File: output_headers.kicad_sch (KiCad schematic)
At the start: 1 part, among them J3 171857-0003

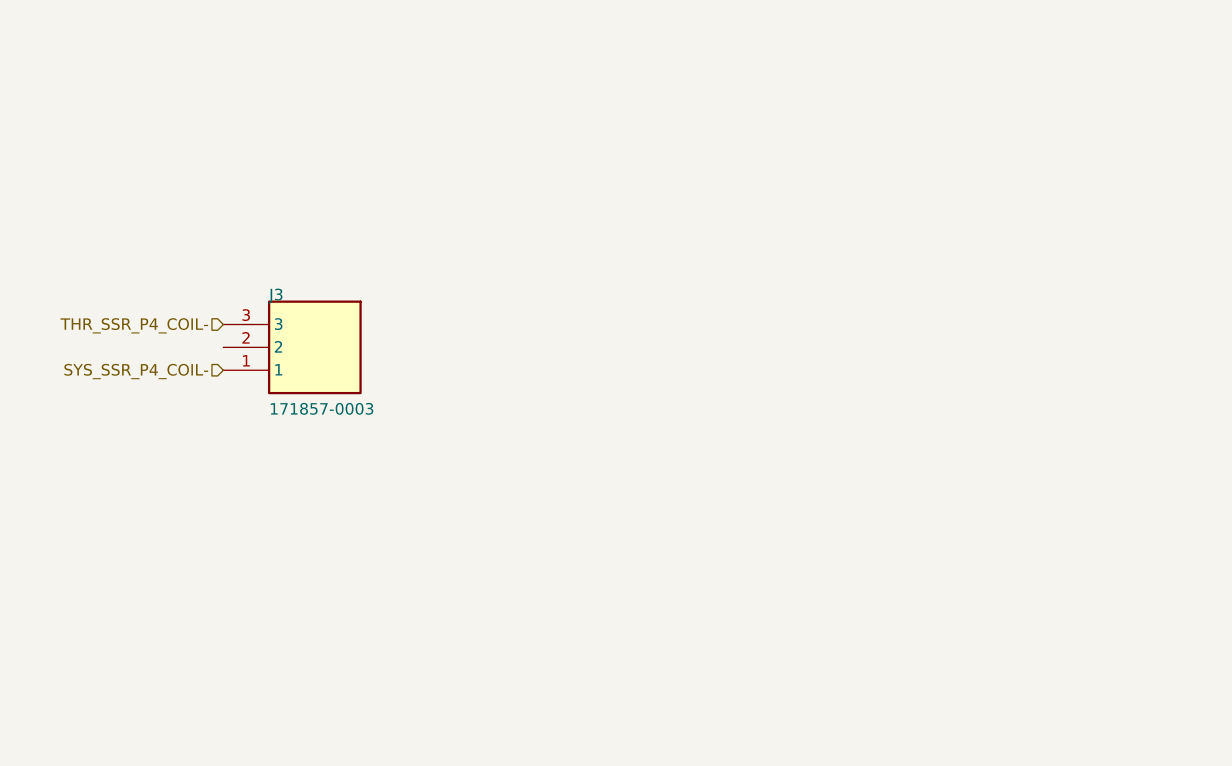
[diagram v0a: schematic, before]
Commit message: Finished updating all input and output headers
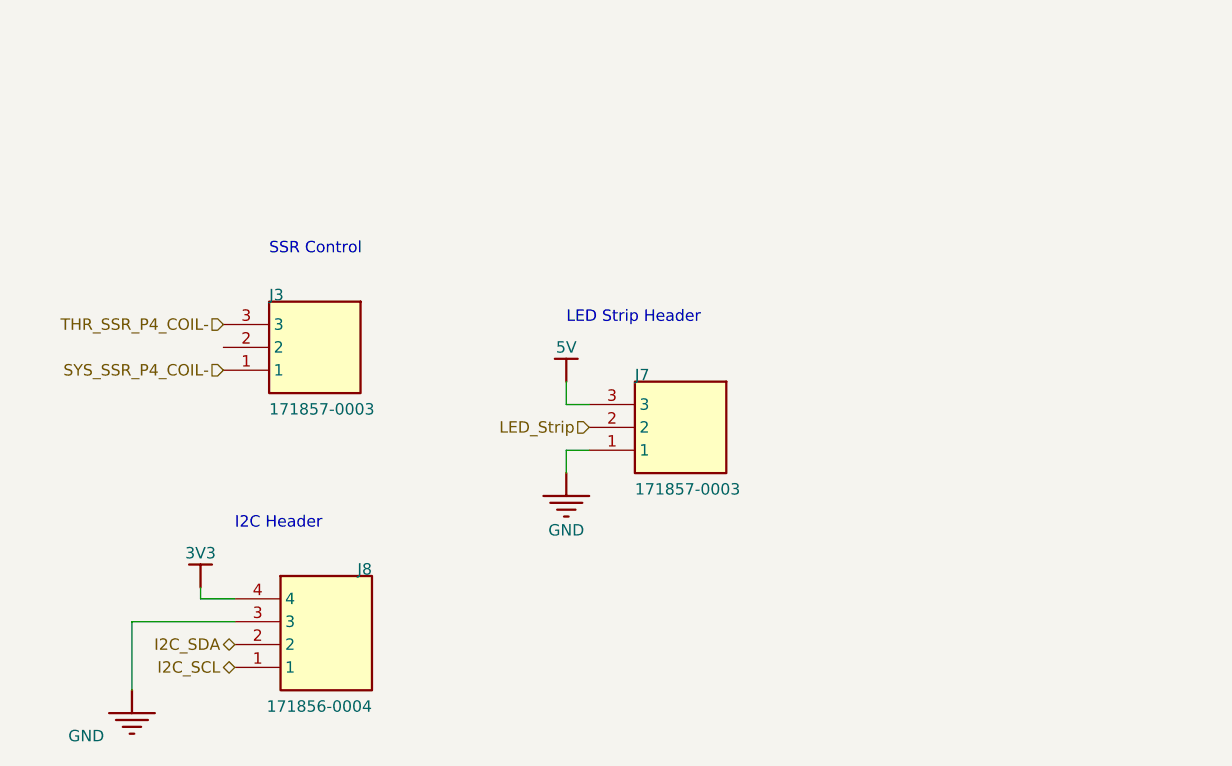
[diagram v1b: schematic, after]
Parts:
- added J7: 171857-0003, AltiumImport:171857-0003, symbol MEB-altium-import:root_0_171857-0003
- added J8: 171856-0004, AltiumImport:SHDR4W99P0X254_1X4_1001X635X1105P, symbol MEB-altium-import:root_2_171856-0004
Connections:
- new net 3V3: J8.4
- new net 5V: J7.3
- new net GND: J7.1, J8.3
- new net I2C_SCL: J8.1
- new net I2C_SDA: J8.2
- new net LED_Strip: J7.2
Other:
- note added: "I2C Header"
- note added: "LED Strip Header"
- note added: "SSR Control"
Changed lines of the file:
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@@
 (kicad_sch (version 20230121) (generator eeschema)
   (paper "A4")
+  (wire (pts (xy 110.49 116.84) (xy 110.49 119.38))
+    (stroke (width 0.254) (type default))
+  )
+  (wire (pts (xy 110.49 109.22) (xy 110.49 111.76))
+    (stroke (width 0.254) (type default))
+  )
+  (wire (pts (xy 69.85 132.08) (xy 69.85 133.35))
+    (stroke (width 0) (type default))
+  )
+  (wire (pts (xy 110.49 111.76) (xy 113.03 111.76))
+    (stroke (width 0.254) (type default))
+  )
+  (wire (pts (xy 113.03 116.84) (xy 110.49 116.84))
+    (stroke (width 0.254) (type default))
+  )
+  (wire (pts (xy 62.23 143.51) (xy 62.23 135.89))
+    (stroke (width 0) (type default))
+  )
+  (wire (pts (xy 73.66 133.35) (xy 69.85 133.35))
+    (stroke (width 0) (type default))
+  )
+  (wire (pts (xy 62.23 135.89) (xy 73.66 135.89))
+    (stroke (width 0) (type default))
+  )
+  (text "SSR Control" (at 77.47 95.25 0)
+    (effects (font (size 1.27 1.27)) (justify left bottom))
+  )
+  (text "LED Strip Header" (at 110.49 102.87 0)
+    (effects (font (size 1.27 1.27)) (justify left bottom))
+  )
+  (text "I2C Header" (at 73.66 125.73 0)
+    (effects (font (size 1.27 1.27)) (justify left bottom))
+  )
+  (hierarchical_label "I2C_SCL" (shape bidirectional) (at 73.66 140.97 180) (fields_autoplaced)
+    (effects (font (size 1.27 1.27)) (justify right))
+  )
   (hierarchical_label "SYS_SSR_P4_COIL-" (shape input) (at 72.39 107.95 180) (fields_autoplaced)
     (effects (font (size 1.27 1.27)) (justify right))
@@
     (effects (font (size 1.27 1.27)) (justify right))
   )
-  (symbol (lib_id "MEB-altium-import:system_SSR_control_0_171857-0003") (at 72.39 102.87 0) (unit 1)
-    (in_bom yes) (on_board yes) (dnp no)
-    (property "Reference" "J3" (at 77.47 100.33 0)
-      (effects (font (size 1.27 1.27)) (justify left bottom))
-    )
-    (property "Value" "171857-0003" (at 77.47 113.03 0)
-      (effects (font (size 1.27 1.27)) (justify left bottom))
-    )
-    (property "Footprint" "AltiumImport:171857-0003" (at 72.39 102.87 0)
-      (effects (font (size 1.27 1.27)) hide)
-    )
-    (property "Datasheet" "" (at 72.39 102.87 0)
-      (effects (font (size 1.27 1.27)) hide)
-    )
-    (property "Part Number" "171857-0003" (at 72.39 102.87 0)
+  (hierarchical_label "LED_Strip" (shape input) (at 113.03 114.3 180) (fields_autoplaced)
+    (effects (font (size 1.27 1.27)) (justify right))
+  )
+  (hierarchical_label "I2C_SDA" (shape bidirectional) (at 73.66 138.43 180) (fields_autoplaced)
+    (effects (font (size 1.27 1.27)) (justify right))
+  )
+  (symbol (lib_id "MEB-altium-import:root_2_171856-0004") (at 73.66 140.97 0) (mirror y) (unit 1)
+    (in_bom yes) (on_board yes) (dnp no)
+    (property "Reference" "J8" (at 88.9 130.81 0)
+      (effects (font (size 1.27 1.27)) (justify left bottom))
+    )
+    (property "Value" "171856-0004" (at 88.9 146.05 0)
+      (effects (font (size 1.27 1.27)) (justify left bottom))
+    )
+    (property "Footprint" "AltiumImport:SHDR4W99P0X254_1X4_1001X635X1105P" (at 73.66 140.97 0)
+      (effects (font (size 1.27 1.27)) hide)
+    )
+    (property "Datasheet" "" (at 73.66 140.97 0)
+      (effects (font (size 1.27 1.27)) hide)
+    )
+    (property "Part Number" "171856-0004" (at 73.66 140.97 0)
       (effects (font (size 1.27 1.27)) hide)
     )
@@
     (pin "2")
     (pin "3")
+    (pin "4")
+    (instances
+      (project "MEB"
+        (path "/228e4997-23c1-4c21-939b-583cad26a5e3"
+          (reference "J8") (unit 1)
+        )
+        (path "/228e4997-23c1-4c21-939b-583cad26a5e3/31cf28dd-aa46-4d0d-9cc3-216a5d7181ad"
+          (reference "J5") (unit 1)
+        )
+      )
+    )
+  )
+  (symbol (lib_id "MEB-altium-import:GND") (at 62.23 143.51 0) (unit 1)
+    (in_bom yes) (on_board yes) (dnp no)
+    (property "Reference" "#PWR01" (at 57.15 143.51 0)
+      (effects (font (size 1.27 1.27)) hide)
+    )
+    (property "Value" "GND" (at 57.15 148.59 0)
+      (effects (font (size 1.27 1.27)))
+    )
+    (property "Footprint" "" (at 62.23 143.51 0)
+      (effects (font (size 1.27 1.27)) hide)
+    )
+    (property "Datasheet" "" (at 62.23 143.51 0)
+      (effects (font (size 1.27 1.27)) hide)
+    )
+    (pin "")
+    (instances
+      (project "MEB"
+        (path "/228e4997-23c1-4c21-939b-583cad26a5e3/3aab6a70-cc66-4393-a750-92acad576aaa"
+          (reference "#PWR01") (unit 1)
+        )
+        (path "/228e4997-23c1-4c21-939b-583cad26a5e3/31cf28dd-aa46-4d0d-9cc3-216a5d7181ad"
+          (reference "#PWR05") (unit 1)
+        )
+      )
+    )
+  )
+  (symbol (lib_id "MEB-altium-import:GND") (at 110.49 119.38 0) (unit 1)
+    (in_bom yes) (on_board yes) (dnp no)
+    (property "Reference" "#PWR0106" (at 110.49 119.38 0)
+      (effects (font (size 1.27 1.27)) hide)
+    )
+    (property "Value" "GND" (at 110.49 125.73 0)
+      (effects (font (size 1.27 1.27)))
+    )
+    (property "Footprint" "" (at 110.49 119.38 0)
+      (effects (font (size 1.27 1.27)) hide)
+    )
+    (property "Datasheet" "" (at 110.49 119.38 0)
+      (effects (font (size 1.27 1.27)) hide)
+    )
+    (pin "")
+    (instances
+      (project "MEB"
+        (path "/228e4997-23c1-4c21-939b-583cad26a5e3"
+          (reference "#PWR0106") (unit 1)
+        )
+        (path "/228e4997-23c1-4c21-939b-583cad26a5e3/31cf28dd-aa46-4d0d-9cc3-216a5d7181ad"
+          (reference "#PWR08") (unit 1)
+        )
+      )
+    )
+  )
+  (symbol (lib_id "MEB-altium-import:root_0_171857-0003") (at 113.03 111.76 0) (unit 1)
+    (in_bom yes) (on_board yes) (dnp no)
+    (property "Reference" "J7" (at 118.11 109.22 0)
+      (effects (font (size 1.27 1.27)) (justify left bottom))
+    )
+    (property "Value" "171857-0003" (at 118.11 121.92 0)
+      (effects (font (size 1.27 1.27)) (justify left bottom))
+    )
+    (property "Footprint" "AltiumImport:171857-0003" (at 113.03 111.76 0)
+      (effects (font (size 1.27 1.27)) hide)
+    )
+    (property "Datasheet" "" (at 113.03 111.76 0)
+      (effects (font (size 1.27 1.27)) hide)
+    )
+    (property "Part Number" "171857-0003" (at 113.03 111.76 0)
+      (effects (font (size 1.27 1.27)) hide)
+    )
+    (pin "1")
+    (pin "2")
+    (pin "3")
+    (instances
+      (project "MEB"
+        (path "/228e4997-23c1-4c21-939b-583cad26a5e3"
+          (reference "J7") (unit 1)
+        )
+        (path "/228e4997-23c1-4c21-939b-583cad26a5e3/31cf28dd-aa46-4d0d-9cc3-216a5d7181ad"
+          (reference "J6") (unit 1)
+        )
+      )
+    )
+  )
+  (symbol (lib_id "MEB-altium-import:system_SSR_control_0_171857-0003") (at 72.39 102.87 0) (unit 1)
+    (in_bom yes) (on_board yes) (dnp no)
+    (property "Reference" "J3" (at 77.47 100.33 0)
+      (effects (font (size 1.27 1.27)) (justify left bottom))
+    )
+    (property "Value" "171857-0003" (at 77.47 113.03 0)
+      (effects (font (size 1.27 1.27)) (justify left bottom))
+    )
+    (property "Footprint" "AltiumImport:171857-0003" (at 72.39 102.87 0)
+      (effects (font (size 1.27 1.27)) hide)
+    )
+    (property "Datasheet" "" (at 72.39 102.87 0)
+      (effects (font (size 1.27 1.27)) hide)
+    )
+    (property "Part Number" "171857-0003" (at 72.39 102.87 0)
+      (effects (font (size 1.27 1.27)) hide)
+    )
+    (pin "1")
+    (pin "2")
+    (pin "3")
     (instances
       (project "MEB"
@@
         )
       )
+    )
+  )
+  (symbol (lib_id "MEB-altium-import:3V3") (at 69.85 132.08 180) (unit 1)
+    (in_bom yes) (on_board yes) (dnp no)
+    (property "Reference" "#PWR0107" (at 69.85 132.08 0)
+      (effects (font (size 1.27 1.27)) hide)
+    )
+    (property "Value" "3V3" (at 69.85 128.27 0)
+      (effects (font (size 1.27 1.27)))
+    )
+    (property "Footprint" "" (at 69.85 132.08 0)
+      (effects (font (size 1.27 1.27)) hide)
+    )
+    (property "Datasheet" "" (at 69.85 132.08 0)
+      (effects (font (size 1.27 1.27)) hide)
+    )
+    (pin "")
+    (instances
+      (project "MEB"
+        (path "/228e4997-23c1-4c21-939b-583cad26a5e3"
+          (reference "#PWR0107") (unit 1)
+        )
+        (path "/228e4997-23c1-4c21-939b-583cad26a5e3/31cf28dd-aa46-4d0d-9cc3-216a5d7181ad"
+          (reference "#PWR06") (unit 1)
+        )
+      )
+    )
+  )
+  (symbol (lib_id "MEB-altium-import:5V") (at 110.49 109.22 180) (unit 1)
+    (in_bom yes) (on_board yes) (dnp no)
+    (property "Reference" "#PWR0105" (at 110.49 109.22 0)
+      (effects (font (size 1.27 1.27)) hide)
+    )
+    (property "Value" "5V" (at 110.49 105.41 0)
+      (effects (font (size 1.27 1.27)))
+    )
+    (property "Footprint" "" (at 110.49 109.22 0)
+      (effects (font (size 1.27 1.27)) hide)
+    )
+    (property "Datasheet" "" (at 110.49 109.22 0)
+      (effects (font (size 1.27 1.27)) hide)
+    )
+    (pin "")
+    (instances
+      (project "MEB"
+        (path "/228e4997-23c1-4c21-939b-583cad26a5e3"
+          (reference "#PWR0105") (unit 1)
+        )
+        (path "/228e4997-23c1-4c21-939b-583cad26a5e3/31cf28dd-aa46-4d0d-9cc3-216a5d7181ad"
+          (reference "#PWR07") (unit 1)
+        )
+      )

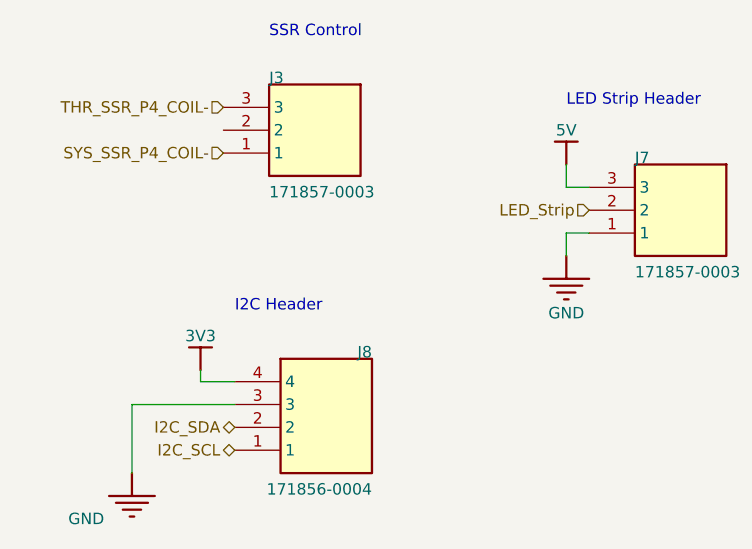
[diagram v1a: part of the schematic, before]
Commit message: updated power and ground symbols in schematic to kicad library version
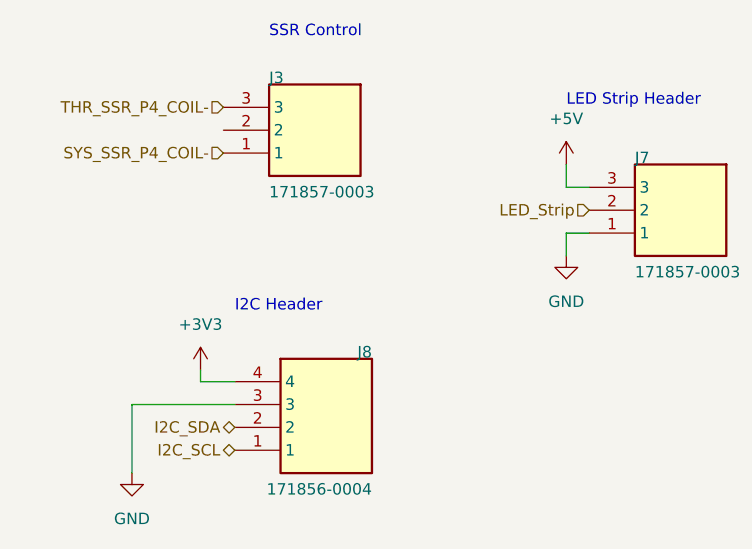
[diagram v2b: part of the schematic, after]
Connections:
- net 3V3 renamed +3V3
- net 5V renamed +5V
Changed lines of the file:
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@@
     (effects (font (size 1.27 1.27)) (justify right))
+  )
+  (symbol (lib_id "power:+5V") (at 110.49 109.22 0) (unit 1)
+    (in_bom yes) (on_board yes) (dnp no) (fields_autoplaced)
+    (property "Reference" "#PWR028" (at 110.49 113.03 0)
+      (effects (font (size 1.27 1.27)) hide)
+    )
+    (property "Value" "+5V" (at 110.49 104.14 0)
+      (effects (font (size 1.27 1.27)))
+    )
+    (property "Footprint" "" (at 110.49 109.22 0)
+      (effects (font (size 1.27 1.27)) hide)
+    )
+    (property "Datasheet" "" (at 110.49 109.22 0)
+      (effects (font (size 1.27 1.27)) hide)
+    )
+    (pin "1")
+    (instances
+      (project "MEB"
+        (path "/228e4997-23c1-4c21-939b-583cad26a5e3"
+          (reference "#PWR028") (unit 1)
+        )
+        (path "/228e4997-23c1-4c21-939b-583cad26a5e3/31cf28dd-aa46-4d0d-9cc3-216a5d7181ad"
+          (reference "#PWR07") (unit 1)
+        )
+      )
+    )
   )
   (symbol (lib_id "MEB-altium-import:root_2_171856-0004") (at 73.66 140.97 0) (mirror y) (unit 1)
@@
         (path "/228e4997-23c1-4c21-939b-583cad26a5e3/31cf28dd-aa46-4d0d-9cc3-216a5d7181ad"
           (reference "J5") (unit 1)
-        )
-      )
-    )
-  )
-  (symbol (lib_id "MEB-altium-import:GND") (at 62.23 143.51 0) (unit 1)
-    (in_bom yes) (on_board yes) (dnp no)
-    (property "Reference" "#PWR01" (at 57.15 143.51 0)
-      (effects (font (size 1.27 1.27)) hide)
-    )
-    (property "Value" "GND" (at 57.15 148.59 0)
-      (effects (font (size 1.27 1.27)))
-    )
-    (property "Footprint" "" (at 62.23 143.51 0)
-      (effects (font (size 1.27 1.27)) hide)
-    )
-    (property "Datasheet" "" (at 62.23 143.51 0)
-      (effects (font (size 1.27 1.27)) hide)
-    )
-    (pin "")
-    (instances
-      (project "MEB"
-        (path "/228e4997-23c1-4c21-939b-583cad26a5e3/3aab6a70-cc66-4393-a750-92acad576aaa"
-          (reference "#PWR01") (unit 1)
-        )
-        (path "/228e4997-23c1-4c21-939b-583cad26a5e3/31cf28dd-aa46-4d0d-9cc3-216a5d7181ad"
-          (reference "#PWR05") (unit 1)
-        )
-      )
-    )
-  )
-  (symbol (lib_id "MEB-altium-import:GND") (at 110.49 119.38 0) (unit 1)
-    (in_bom yes) (on_board yes) (dnp no)
-    (property "Reference" "#PWR0106" (at 110.49 119.38 0)
-      (effects (font (size 1.27 1.27)) hide)
-    )
-    (property "Value" "GND" (at 110.49 125.73 0)
-      (effects (font (size 1.27 1.27)))
-    )
-    (property "Footprint" "" (at 110.49 119.38 0)
-      (effects (font (size 1.27 1.27)) hide)
-    )
-    (property "Datasheet" "" (at 110.49 119.38 0)
-      (effects (font (size 1.27 1.27)) hide)
-    )
-    (pin "")
-    (instances
-      (project "MEB"
-        (path "/228e4997-23c1-4c21-939b-583cad26a5e3"
-          (reference "#PWR0106") (unit 1)
-        )
-        (path "/228e4997-23c1-4c21-939b-583cad26a5e3/31cf28dd-aa46-4d0d-9cc3-216a5d7181ad"
-          (reference "#PWR08") (unit 1)
         )
       )
@@
     )
   )
-  (symbol (lib_id "MEB-altium-import:3V3") (at 69.85 132.08 180) (unit 1)
-    (in_bom yes) (on_board yes) (dnp no)
-    (property "Reference" "#PWR0107" (at 69.85 132.08 0)
+  (symbol (lib_id "power:GND") (at 62.23 143.51 0) (unit 1)
+    (in_bom yes) (on_board yes) (dnp no) (fields_autoplaced)
+    (property "Reference" "#PWR030" (at 62.23 149.86 0)
       (effects (font (size 1.27 1.27)) hide)
     )
-    (property "Value" "3V3" (at 69.85 128.27 0)
+    (property "Value" "GND" (at 62.23 148.59 0)
+      (effects (font (size 1.27 1.27)))
+    )
+    (property "Footprint" "" (at 62.23 143.51 0)
+      (effects (font (size 1.27 1.27)) hide)
+    )
+    (property "Datasheet" "" (at 62.23 143.51 0)
+      (effects (font (size 1.27 1.27)) hide)
+    )
+    (pin "1")
+    (instances
+      (project "MEB"
+        (path "/228e4997-23c1-4c21-939b-583cad26a5e3/3aab6a70-cc66-4393-a750-92acad576aaa"
+          (reference "#PWR030") (unit 1)
+        )
+        (path "/228e4997-23c1-4c21-939b-583cad26a5e3/31cf28dd-aa46-4d0d-9cc3-216a5d7181ad"
+          (reference "#PWR05") (unit 1)
+        )
+      )
+    )
+  )
+  (symbol (lib_id "power:GND") (at 110.49 119.38 0) (unit 1)
+    (in_bom yes) (on_board yes) (dnp no) (fields_autoplaced)
+    (property "Reference" "#PWR030" (at 110.49 125.73 0)
+      (effects (font (size 1.27 1.27)) hide)
+    )
+    (property "Value" "GND" (at 110.49 124.46 0)
+      (effects (font (size 1.27 1.27)))
+    )
+    (property "Footprint" "" (at 110.49 119.38 0)
+      (effects (font (size 1.27 1.27)) hide)
+    )
+    (property "Datasheet" "" (at 110.49 119.38 0)
+      (effects (font (size 1.27 1.27)) hide)
+    )
+    (pin "1")
+    (instances
+      (project "MEB"
+        (path "/228e4997-23c1-4c21-939b-583cad26a5e3/3aab6a70-cc66-4393-a750-92acad576aaa"
+          (reference "#PWR030") (unit 1)
+        )
+        (path "/228e4997-23c1-4c21-939b-583cad26a5e3/31cf28dd-aa46-4d0d-9cc3-216a5d7181ad"
+          (reference "#PWR08") (unit 1)
+        )
+      )
+    )
+  )
+  (symbol (lib_id "power:+3V3") (at 69.85 132.08 0) (unit 1)
+    (in_bom yes) (on_board yes) (dnp no) (fields_autoplaced)
+    (property "Reference" "#PWR036" (at 69.85 135.89 0)
+      (effects (font (size 1.27 1.27)) hide)
+    )
+    (property "Value" "+3V3" (at 69.85 127 0)
       (effects (font (size 1.27 1.27)))
     )
@@
       (effects (font (size 1.27 1.27)) hide)
     )
-    (pin "")
+    (pin "1")
     (instances
       (project "MEB"
         (path "/228e4997-23c1-4c21-939b-583cad26a5e3"
-          (reference "#PWR0107") (unit 1)
+          (reference "#PWR036") (unit 1)
         )
         (path "/228e4997-23c1-4c21-939b-583cad26a5e3/31cf28dd-aa46-4d0d-9cc3-216a5d7181ad"
@@
         )
       )
-    )
-  )
-  (symbol (lib_id "MEB-altium-import:5V") (at 110.49 109.22 180) (unit 1)
-    (in_bom yes) (on_board yes) (dnp no)
-    (property "Reference" "#PWR0105" (at 110.49 109.22 0)
-      (effects (font (size 1.27 1.27)) hide)
-    )
-    (property "Value" "5V" (at 110.49 105.41 0)
-      (effects (font (size 1.27 1.27)))
-    )
-    (property "Footprint" "" (at 110.49 109.22 0)
-      (effects (font (size 1.27 1.27)) hide)
-    )
-    (property "Datasheet" "" (at 110.49 109.22 0)
-      (effects (font (size 1.27 1.27)) hide)
-    )
-    (pin "")
-    (instances
-      (project "MEB"
-        (path "/228e4997-23c1-4c21-939b-583cad26a5e3"
-          (reference "#PWR0105") (unit 1)
-        )
-        (path "/228e4997-23c1-4c21-939b-583cad26a5e3/31cf28dd-aa46-4d0d-9cc3-216a5d7181ad"
-          (reference "#PWR07") (unit 1)
-        )
-      )

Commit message: Fix a variety of small issues
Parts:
- renumbered J8 to J5, J7 to J6
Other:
- moved on the sheet: J3, J5, J6
